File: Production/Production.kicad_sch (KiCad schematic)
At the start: 28 parts, among them IC1 MAX3323EEPE+, IC2 AP7375-33SA-7, J1 530480510, J2 530480410, J3 USB4085-GF-A_REVB, U2 ADR02AUJZ-REEL7, U3 ATSAMD21G18A-AUT, Y1 32.768, 12.5pF

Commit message: Reloaded footprints & models after switching back to mac
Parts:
- C4: footprint Capacitor_SMD:C_0402_1005Metric -> Capacitor_SMD:C_0805_2012Metric
- J1: footprint Connector_Molex_2:Molex_PicoBlade_53048-0510_1x05_P1.25mm_Horizontal -> Connector_Molex:Molex_PicoBlade_53048-0510_1x05_P1.25mm_Horizontal
- J2: footprint Connector_Molex_2:Molex_PicoBlade_53048-0410_1x04_P1.25mm_Horizontal -> Connector_Molex:Molex_PicoBlade_53048-0410_1x04_P1.25mm_Horizontal
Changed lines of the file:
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@@
 		)
 		(instances
-			(project "Standalone"
+			(project "Production"
 				(path "/36880c03-5560-4777-bc12-f18c70ba2db4"
 					(reference "#PWR011")
@@
 		)
 		(instances
-			(project ""
+			(project "Production"
 				(path "/36880c03-5560-4777-bc12-f18c70ba2db4"
 					(reference "IC2")
@@
 		)
 		(instances
-			(project "Standalone"
+			(project "Production"
 				(path "/36880c03-5560-4777-bc12-f18c70ba2db4"
 					(reference "#PWR014")
@@
 			)
 		)
-		(property "Footprint" "Connector_Molex_2:Molex_PicoBlade_53048-0510_1x05_P1.25mm_Horizontal"
+		(property "Footprint" "Connector_Molex:Molex_PicoBlade_53048-0510_1x05_P1.25mm_Horizontal"
 			(at 54.61 54.61 0)
 			(effects
@@
 		)
 		(instances
-			(project "Standalone"
+			(project "Production"
 				(path "/36880c03-5560-4777-bc12-f18c70ba2db4"
 					(reference "J1")
@@
 		)
 		(instances
-			(project "Standalone"
+			(project "Production"
 				(path "/36880c03-5560-4777-bc12-f18c70ba2db4"
 					(reference "D4")
@@
 		)
 		(instances
-			(project "Standalone"
+			(project "Production"
 				(path "/36880c03-5560-4777-bc12-f18c70ba2db4"
 					(reference "#PWR018")
@@
 		)
 		(instances
-			(project "Standalone"
+			(project "Production"
 				(path "/36880c03-5560-4777-bc12-f18c70ba2db4"
 					(reference "#PWR08")
@@
 		)
 		(instances
-			(project "Standalone"
+			(project "Production"
 				(path "/36880c03-5560-4777-bc12-f18c70ba2db4"
 					(reference "#PWR03")
@@
 		)
 		(instances
-			(project "Standalone"
+			(project "Production"
 				(path "/36880c03-5560-4777-bc12-f18c70ba2db4"
 					(reference "C8")
@@
 		)
 		(instances
-			(project "Standalone"
+			(project "Production"
 				(path "/36880c03-5560-4777-bc12-f18c70ba2db4"
 					(reference "#PWR021")
@@
 		)
 		(instances
-			(project "Standalone"
+			(project "Production"
 				(path "/36880c03-5560-4777-bc12-f18c70ba2db4"
 					(reference "#PWR026")
@@
 		)
 		(instances
-			(project "Standalone"
+			(project "Production"
 				(path "/36880c03-5560-4777-bc12-f18c70ba2db4"
 					(reference "IC1")
@@
 		)
 		(instances
-			(project "Standalone"
+			(project "Production"
 				(path "/36880c03-5560-4777-bc12-f18c70ba2db4"
 					(reference "#PWR022")
@@
 		)
 		(instances
-			(project "Standalone"
+			(project "Production"
 				(path "/36880c03-5560-4777-bc12-f18c70ba2db4"
 					(reference "#PWR024")
@@
 		)
 		(instances
-			(project "Standalone"
+			(project "Production"
 				(path "/36880c03-5560-4777-bc12-f18c70ba2db4"
 					(reference "U2")
@@
 		)
 		(instances
-			(project "Standalone"
+			(project "Production"
 				(path "/36880c03-5560-4777-bc12-f18c70ba2db4"
 					(reference "#PWR016")
@@
 		)
 		(instances
-			(project "Standalone"
+			(project "Production"
 				(path "/36880c03-5560-4777-bc12-f18c70ba2db4"
 					(reference "C2")
@@
 		)
 		(instances
-			(project "Standalone"
+			(project "Production"
 				(path "/36880c03-5560-4777-bc12-f18c70ba2db4"
 					(reference "J3")
@@
 			)
 		)
-		(property "Footprint" "Capacitor_SMD:C_0402_1005Metric"
+		(property "Footprint" "Capacitor_SMD:C_0805_2012Metric"
 			(at 114.6048 39.37 0)
 			(effects
@@
 		)
 		(instances
-			(project "Standalone"
+			(project "Production"
 				(path "/36880c03-5560-4777-bc12-f18c70ba2db4"
 					(reference "C4")
@@
 		)
 		(instances
-			(project "Standalone"
+			(project "Production"
 				(path "/36880c03-5560-4777-bc12-f18c70ba2db4"
 					(reference "R2")
@@
 		)
 		(instances
-			(project "Standalone"
+			(project "Production"
 				(path "/36880c03-5560-4777-bc12-f18c70ba2db4"
 					(reference "#PWR039")
@@
 		)
 		(instances
-			(project "Standalone"
+			(project "Production"
 				(path "/36880c03-5560-4777-bc12-f18c70ba2db4"
 					(reference "#PWR013")
@@
 		)
 		(instances
-			(project "Standalone"
+			(project "Production"
 				(path "/36880c03-5560-4777-bc12-f18c70ba2db4"
 					(reference "D1")
@@
 		)
 		(instances
-			(project "Standalone"
+			(project "Production"
 				(path "/36880c03-5560-4777-bc12-f18c70ba2db4"
 					(reference "#PWR06")
@@
 		)
 		(instances
-			(project "Standalone"
+			(project "Production"
 				(path "/36880c03-5560-4777-bc12-f18c70ba2db4"
 					(reference "#PWR07")
@@
 		)
 		(instances
-			(project "Standalone"
+			(project "Production"
 				(path "/36880c03-5560-4777-bc12-f18c70ba2db4"
 					(reference "D2")
@@
 		)
 		(instances
-			(project "Standalone"
+			(project "Production"
 				(path "/36880c03-5560-4777-bc12-f18c70ba2db4"
 					(reference "#PWR015")
@@
 		)
 		(instances
-			(project "Standalone"
+			(project "Production"
 				(path "/36880c03-5560-4777-bc12-f18c70ba2db4"
 					(reference "#PWR020")
@@
 		)
 		(instances
-			(project "Standalone"
+			(project "Production"
 				(path "/36880c03-5560-4777-bc12-f18c70ba2db4"
 					(reference "#PWR017")
@@
 		)
 		(instances
-			(project "Standalone"
+			(project "Production"
 				(path "/36880c03-5560-4777-bc12-f18c70ba2db4"
 					(reference "R1")
@@
 		)
 		(instances
-			(project ""
+			(project "Production"
 				(path "/36880c03-5560-4777-bc12-f18c70ba2db4"
 					(reference "S1")
@@
 		)
 		(instances
-			(project "Standalone"
+			(project "Production"
 				(path "/36880c03-5560-4777-bc12-f18c70ba2db4"
 					(reference "#PWR02")
@@
 		)
 		(instances
-			(project "Standalone"
+			(project "Production"
 				(path "/36880c03-5560-4777-bc12-f18c70ba2db4"
 					(reference "#PWR04")
@@
 		)
 		(instances
-			(project "Standalone"
+			(project "Production"
 				(path "/36880c03-5560-4777-bc12-f18c70ba2db4"
 					(reference "R8")
@@
 		)
 		(instances
-			(project "Standalone"
+			(project "Production"
 				(path "/36880c03-5560-4777-bc12-f18c70ba2db4"
 					(reference "C5")
@@
 		)
 		(instances
-			(project ""
+			(project "Production"
 				(path "/36880c03-5560-4777-bc12-f18c70ba2db4"
 					(reference "RESET1")
@@
 		)
 		(instances
-			(project "Standalone"
+			(project "Production"
 				(path "/36880c03-5560-4777-bc12-f18c70ba2db4"
 					(reference "C1")
@@
 		)
 		(instances
-			(project "Standalone"
+			(project "Production"
 				(path "/36880c03-5560-4777-bc12-f18c70ba2db4"
 					(reference "#PWR01")
@@
 		)
 		(instances
-			(project "Standalone"
+			(project "Production"
 				(path "/36880c03-5560-4777-bc12-f18c70ba2db4"
 					(reference "R3")
@@
 		)
 		(instances
-			(project "Standalone"
+			(project "Production"
 				(path "/36880c03-5560-4777-bc12-f18c70ba2db4"
 					(reference "#PWR010")
@@
 		)
 		(instances
-			(project "Standalone"
+			(project "Production"
 				(path "/36880c03-5560-4777-bc12-f18c70ba2db4"
 					(reference "R5")
@@
 		)
 		(instances
-			(project "Standalone"
+			(project "Production"
 				(path "/36880c03-5560-4777-bc12-f18c70ba2db4"
 					(reference "C6")
@@
 		)
 		(instances
-			(project "Standalone"
+			(project "Production"
 				(path "/36880c03-5560-4777-bc12-f18c70ba2db4"
 					(reference "C7")
@@
 		)
 		(instances
-			(project "Standalone"
+			(project "Production"
 				(path "/36880c03-5560-4777-bc12-f18c70ba2db4"
 					(reference "U3")
@@
 		)
 		(instances
-			(project "Standalone"
+			(project "Production"
 				(path "/36880c03-5560-4777-bc12-f18c70ba2db4"
 					(reference "Y1")
@@
 		)
 		(instances
-			(project "Standalone"
+			(project "Production"
 				(path "/36880c03-5560-4777-bc12-f18c70ba2db4"
 					(reference "#PWR023")
@@
 		)
 		(instances
-			(project "Standalone"
+			(project "Production"
 				(path "/36880c03-5560-4777-bc12-f18c70ba2db4"
 					(reference "#PWR09")
@@
 		)
 		(instances
-			(project "Standalone"
+			(project "Production"
 				(path "/36880c03-5560-4777-bc12-f18c70ba2db4"
 					(reference "#PWR012")
@@
 			)
 		)
-		(property "Footprint" "Connector_Molex_2:Molex_PicoBlade_53048-0410_1x04_P1.25mm_Horizontal"
+		(property "Footprint" "Connector_Molex:Molex_PicoBlade_53048-0410_1x04_P1.25mm_Horizontal"
 			(at 54.61 81.28 0)
 			(effects
@@
 		)
 		(instances
-			(project "Standalone"
+			(project "Production"
 				(path "/36880c03-5560-4777-bc12-f18c70ba2db4"
 					(reference "J2")
@@
 		)
 		(instances
-			(project "Standalone"
+			(project "Production"
 				(path "/36880c03-5560-4777-bc12-f18c70ba2db4"
 					(reference "#PWR05")
@@
 		)
 		(instances
-			(project "Standalone"
+			(project "Production"
 				(path "/36880c03-5560-4777-bc12-f18c70ba2db4"
 					(reference "C3")
@@
 		)
 		(instances
-			(project "Standalone"
+			(project "Production"
 				(path "/36880c03-5560-4777-bc12-f18c70ba2db4"
 					(reference "#PWR025")

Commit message: v1, as submitted for production
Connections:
- net SCK: now also U3.12 (PA07); no longer U3.10 (PA05)
- net ZSIG: now also U3.47 (PB02); no longer U3.41 (PA28)
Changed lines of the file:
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@@
-	(wire
-		(pts
-			(xy 256.54 104.14) (xy 260.35 104.14)
-		)
-		(stroke
-			(width 0)
-			(type default)
-		)
-	)
 	(wire
 		(pts
@@
 	(global_label "SCK"
 		(shape input)
-		(at 231.14 88.9 180)
+		(at 231.14 93.98 180)
 		(fields_autoplaced yes)
 		(effects
@@
 		)
 		(property "Intersheetrefs" "${INTERSHEET_REFS}"
-			(at 224.4053 88.9 0)
+			(at 224.4053 93.98 0)
 			(effects
 				(font
@@
 	(global_label "ZSIG"
 		(shape input)
-		(at 260.35 104.14 0)
+		(at 256.54 96.52 0)
 		(fields_autoplaced yes)
 		(effects
@@
 		)
 		(property "Intersheetrefs" "${INTERSHEET_REFS}"
-			(at 267.629 104.14 0)
-			(effects
-				(font
+			(at 263.819 96.52 0)
+			(effects
+				(font

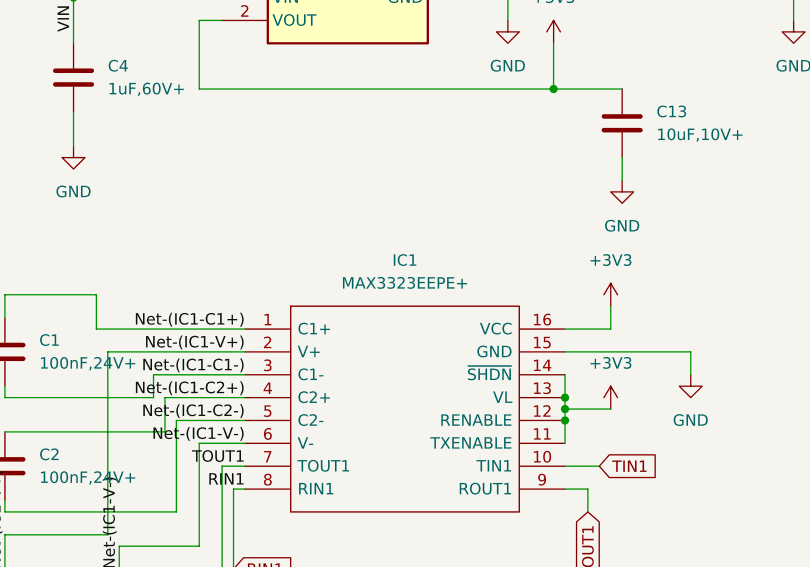
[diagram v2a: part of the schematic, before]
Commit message: Updated BOM to include part numbers
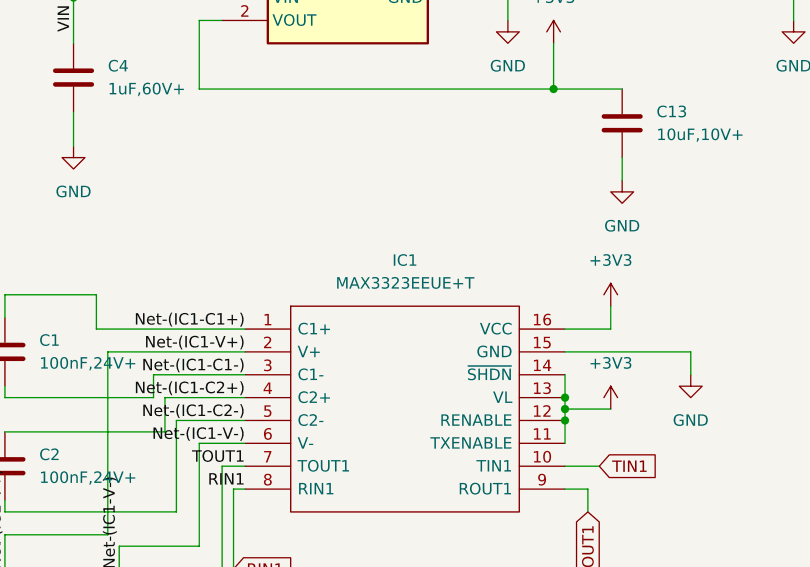
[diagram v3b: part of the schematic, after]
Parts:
- C1, C2, C3, C5: Part Number (none) -> CL05B104KA5NNNC; URL (none) -> https://www.digikey.com/en/products/detail/samsung-electro-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
- C13: Part Number (none) -> CL05A106MP6NUN8; URL (none) -> https://www.digikey.com/en/products/detail/samsung-electro-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
- C4: Part Number (none) -> GRM21BC72A105KE01L; URL (none) -> https://www.digikey.com/en/products/detail/murata-electroni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
- C6, C7: Part Number (none) -> CL05C220JB51PNC; URL (none) -> https://www.digikey.com/en/products/detail/samsung-electro-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
- C8: Part Number (none) -> CL05C010CB5NNNC; URL (none) -> https://www.digikey.com/en/products/detail/samsung-electro-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
- D1, D2: Part Number (none) -> SD1206S100S1R0; URL (none) -> https://www.digikey.com/en/products/detail/kyocera-avx/SD12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
- D4: Part Number (none) -> B1701URO-20D000114U1930; URL (none) -> https://www.digikey.com/en/products/detail/harvatek-corpora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
- IC1: value MAX3323EEPE+ -> MAX3323EEUE+T; Part Number (none) -> MAX3323EEUE+T; URL (none) -> https://www.digikey.com/en/products/detail/analog-devices-i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
- IC2: Part Number (none) -> AP7375-33SA-7; URL (none) -> https://www.digikey.com/en/products/detail/diodes-incorpora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
- J1: Part Number (none) -> 530480510; URL (none) -> https://www.digikey.com/en/products/detail/molex/0530480510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
- J2: Part Number (none) -> 530480410; URL (none) -> https://www.digikey.com/en/products/detail/molex/0530480410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
- J3: Part Number (none) -> USB4085-GF-A; URL (none) -> https://www.digikey.com/en/products/detail/gct/USB4085-GF-A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
- R1, R2: Part Number (none) -> ESR03EZPJ512; URL (none) -> https://www.digikey.com/en/products/detail/rohm-semiconduct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
- R3: Part Number (none) -> RC0603FR-074K7L; URL (none) -> https://www.digikey.com/en/products/detail/yageo/RC0603FR-0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
- R5: Part Number (none) -> RC0603FR-073K3L; URL (none) -> https://www.digikey.com/en/products/detail/yageo/RC0603FR-0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
- R8: Part Number (none) -> RC0603FR-0764R9L; URL (none) -> https://www.digikey.com/en/products/detail/yageo/RC0603FR-0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
- RESET1: Part Number (none) -> B3U-1000P; URL (none) -> https://www.digikey.com/en/products/detail/omron-electronic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
- S1, S2: Part Number (none) -> 1-1825910-4; URL (none) -> https://www.digikey.com/en/products/detail/te-connectivity-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
- U2: Part Number (none) -> ADR02AUJZ-REEL7; URL (none) -> https://www.digikey.com/en/products/detail/analog-devices-i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
- U3: Part Number (none) -> ATSAMD21G18A-AUT; URL (none) -> https://www.digikey.com/en/products/detail/microchip-techno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
- Y1: Part Number (none) -> 32.768K12.5PI/3215E; URL (none) -> https://www.digikey.com/en/products/detail/yic/32-768K12-5P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
